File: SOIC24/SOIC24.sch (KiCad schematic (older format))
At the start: 5 parts, among them J1 Conn_01x12, J2 Conn_02x12_Counter_Clockwise, J3 Conn_02x12_Counter_Clockwise, J4 Conn_02x12_Counter_Clockwise, J5 Conn_01x12

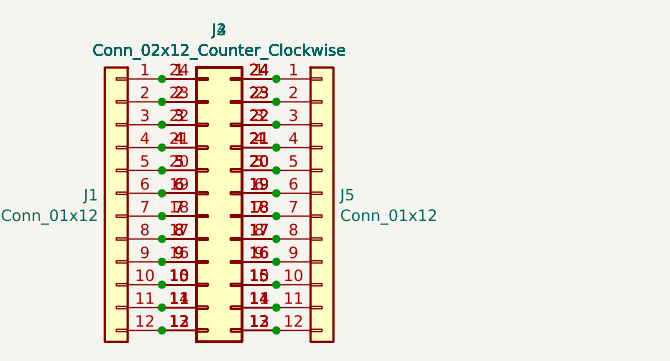
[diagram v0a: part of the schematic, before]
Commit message: Silkscreens and sizes updated
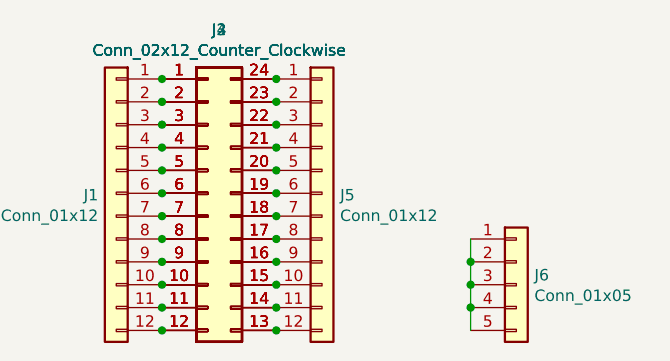
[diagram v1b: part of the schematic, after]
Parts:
- added J6: Conn_01x05, Connector_PinHeader_2.54mm:PinHeader_1x05_P2.54mm_Vertical, symbol Connector_Generic:Conn_01x05
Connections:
- net at J2.24 (Pin_24), J3.24 (Pin_24), J5.1 (Pin_1): now also J4.24 (Pin_24); no longer J4.1 (Pin_1)
- net at J2.15 (Pin_15), J3.15 (Pin_15), J5.10 (Pin_10): now also J4.15 (Pin_15); no longer J4.10 (Pin_10)
- net at J2.14 (Pin_14), J3.14 (Pin_14), J5.11 (Pin_11): now also J4.14 (Pin_14); no longer J4.11 (Pin_11)
- net at J2.13 (Pin_13), J3.13 (Pin_13), J5.12 (Pin_12): now also J4.13 (Pin_13); no longer J4.12 (Pin_12)
- net at J2.23 (Pin_23), J3.23 (Pin_23), J5.2 (Pin_2): now also J4.23 (Pin_23); no longer J4.2 (Pin_2)
- net at J2.22 (Pin_22), J3.22 (Pin_22), J5.3 (Pin_3): now also J4.22 (Pin_22); no longer J4.3 (Pin_3)
- net at J2.21 (Pin_21), J3.21 (Pin_21), J5.4 (Pin_4): now also J4.21 (Pin_21); no longer J4.4 (Pin_4)
- net at J2.20 (Pin_20), J3.20 (Pin_20), J5.5 (Pin_5): now also J4.20 (Pin_20); no longer J4.5 (Pin_5)
- net at J2.19 (Pin_19), J3.19 (Pin_19), J5.6 (Pin_6): now also J4.19 (Pin_19); no longer J4.6 (Pin_6)
- net at J2.18 (Pin_18), J3.18 (Pin_18), J5.7 (Pin_7): now also J4.18 (Pin_18); no longer J4.7 (Pin_7)
- net at J2.17 (Pin_17), J3.17 (Pin_17), J5.8 (Pin_8): now also J4.17 (Pin_17); no longer J4.8 (Pin_8)
- net at J2.16 (Pin_16), J3.16 (Pin_16), J5.9 (Pin_9): now also J4.16 (Pin_16); no longer J4.9 (Pin_9)
- net at J1.1 (Pin_1), J2.1 (Pin_1), J3.1 (Pin_1): now also J4.1 (Pin_1); no longer J4.24 (Pin_24)
- net at J1.10 (Pin_10), J2.10 (Pin_10), J3.10 (Pin_10): now also J4.10 (Pin_10); no longer J4.15 (Pin_15)
- net at J1.11 (Pin_11), J2.11 (Pin_11), J3.11 (Pin_11): now also J4.11 (Pin_11); no longer J4.14 (Pin_14)
- net at J1.12 (Pin_12), J2.12 (Pin_12), J3.12 (Pin_12): now also J4.12 (Pin_12); no longer J4.13 (Pin_13)
- net at J1.2 (Pin_2), J2.2 (Pin_2), J3.2 (Pin_2): now also J4.2 (Pin_2); no longer J4.23 (Pin_23)
- net at J1.3 (Pin_3), J2.3 (Pin_3), J3.3 (Pin_3): now also J4.3 (Pin_3); no longer J4.22 (Pin_22)
- net at J1.4 (Pin_4), J2.4 (Pin_4), J3.4 (Pin_4): now also J4.4 (Pin_4); no longer J4.21 (Pin_21)
- net at J1.5 (Pin_5), J2.5 (Pin_5), J3.5 (Pin_5): now also J4.5 (Pin_5); no longer J4.20 (Pin_20)
- net at J1.6 (Pin_6), J2.6 (Pin_6), J3.6 (Pin_6): now also J4.6 (Pin_6); no longer J4.19 (Pin_19)
- net at J1.7 (Pin_7), J2.7 (Pin_7), J3.7 (Pin_7): now also J4.7 (Pin_7); no longer J4.18 (Pin_18)
- net at J1.8 (Pin_8), J2.8 (Pin_8), J3.8 (Pin_8): now also J4.8 (Pin_8); no longer J4.17 (Pin_17)
- net at J1.9 (Pin_9), J2.9 (Pin_9), J3.9 (Pin_9): now also J4.9 (Pin_9); no longer J4.16 (Pin_16)
- new net: J6.1 (Pin_1), J6.2 (Pin_2), J6.3 (Pin_3), J6.4 (Pin_4), J6.5 (Pin_5)
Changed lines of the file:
@@
 EESchema Schematic File Version 4
-LIBS:SOIC28-cache
+LIBS:SOIC24-cache
 EELAYER 29 0
 EELAYER END
@@
 $EndComp
 $Comp
-L Connector_Generic:Conn_02x12_Counter_Clockwise J4
-U 1 1 5D376A89
-P 6450 3700
-F 0 "J4" H 6500 4415 50  0000 C CNN
-F 1 "Conn_02x12_Counter_Clockwise" H 6500 4325 50  0000 C CNN
-F 2 "Package_DFN_QFN:QFN-24-1EP_5x5mm_P0.65mm_EP3.4x3.4mm" H 6450 3700 50  0001 C CNN
-F 3 "~" H 6450 3700 50  0001 C CNN
-	1    6450 3700
-	-1   0    0    -1
-$EndComp
-$Comp
-L Connector_Generic:Conn_02x12_Counter_Clockwise J2
-U 1 1 5D378DEE
-P 6350 3700
-F 0 "J2" H 6400 4415 50  0000 C CNN
-F 1 "Conn_02x12_Counter_Clockwise" H 6400 4325 50  0000 C CNN
-F 2 "Package_DFN_QFN:QFN-24-1EP_3x3mm_P0.4mm_EP1.75x1.6mm" H 6350 3700 50  0001 C CNN
-F 3 "~" H 6350 3700 50  0001 C CNN
-	1    6350 3700
-	1    0    0    -1
-$EndComp
-$Comp
 L Connector_Generic:Conn_02x12_Counter_Clockwise J3
 U 1 1 5D379B2C
@@
 F 1 "Conn_02x12_Counter_Clockwise" H 6400 4325 50  0000 C CNN
 F 2 "Package_SO:SOIC-24W_7.5x15.4mm_P1.27mm" H 6350 3700 50  0001 C CNN
+F 3 "~" H 6350 3700 50  0001 C CNN
+	1    6350 3700
+	1    0    0    -1
+$EndComp
+$Comp
+L Connector_Generic:Conn_02x12_Counter_Clockwise J2
+U 1 1 5D3AA382
+P 6350 3700
+F 0 "J2" H 6400 4415 50  0000 C CNN
+F 1 "Conn_02x12_Counter_Clockwise" H 6400 4325 50  0000 C CNN
+F 2 "Package_DFN_QFN:QFN-24-1EP_3x3mm_P0.4mm_EP1.75x1.6mm" H 6350 3700 50  0001 C CNN
 F 3 "~" H 6350 3700 50  0001 C CNN
 	1    6350 3700
@@
 Connection ~ 6650 4200
 Connection ~ 6650 4300
+$Comp
+L Connector_Generic:Conn_02x12_Counter_Clockwise J4
+U 1 1 5D3AD66F
+P 6350 3700
+F 0 "J4" H 6400 4415 50  0000 C CNN
+F 1 "Conn_02x12_Counter_Clockwise" H 6400 4325 50  0000 C CNN
+F 2 "Package_DFN_QFN:QFN-24-1EP_5x5mm_P0.65mm_EP3.4x3.4mm" H 6350 3700 50  0001 C CNN
+F 3 "~" H 6350 3700 50  0001 C CNN
+	1    6350 3700
+	1    0    0    -1
+$EndComp
+$Comp
+L Connector_Generic:Conn_01x05 J6
+U 1 1 5D3D3EBE
+P 7700 4100
+F 0 "J6" H 7779 4142 50  0000 L CNN
+F 1 "Conn_01x05" H 7779 4052 50  0000 L CNN
+F 2 "Connector_PinHeader_2.54mm:PinHeader_1x05_P2.54mm_Vertical" H 7700 4100 50  0001 C CNN
+F 3 "~" H 7700 4100 50  0001 C CNN
+	1    7700 4100
+	1    0    0    -1
+$EndComp
+Wire Wire Line
+	7500 4300 7500 4200
+Connection ~ 7500 4000
+Wire Wire Line
+	7500 4000 7500 3900
+Connection ~ 7500 4100
+Wire Wire Line
+	7500 4100 7500 4000
+Connection ~ 7500 4200
+Wire Wire Line
+	7500 4200 7500 4100
 $EndSCHEMATC

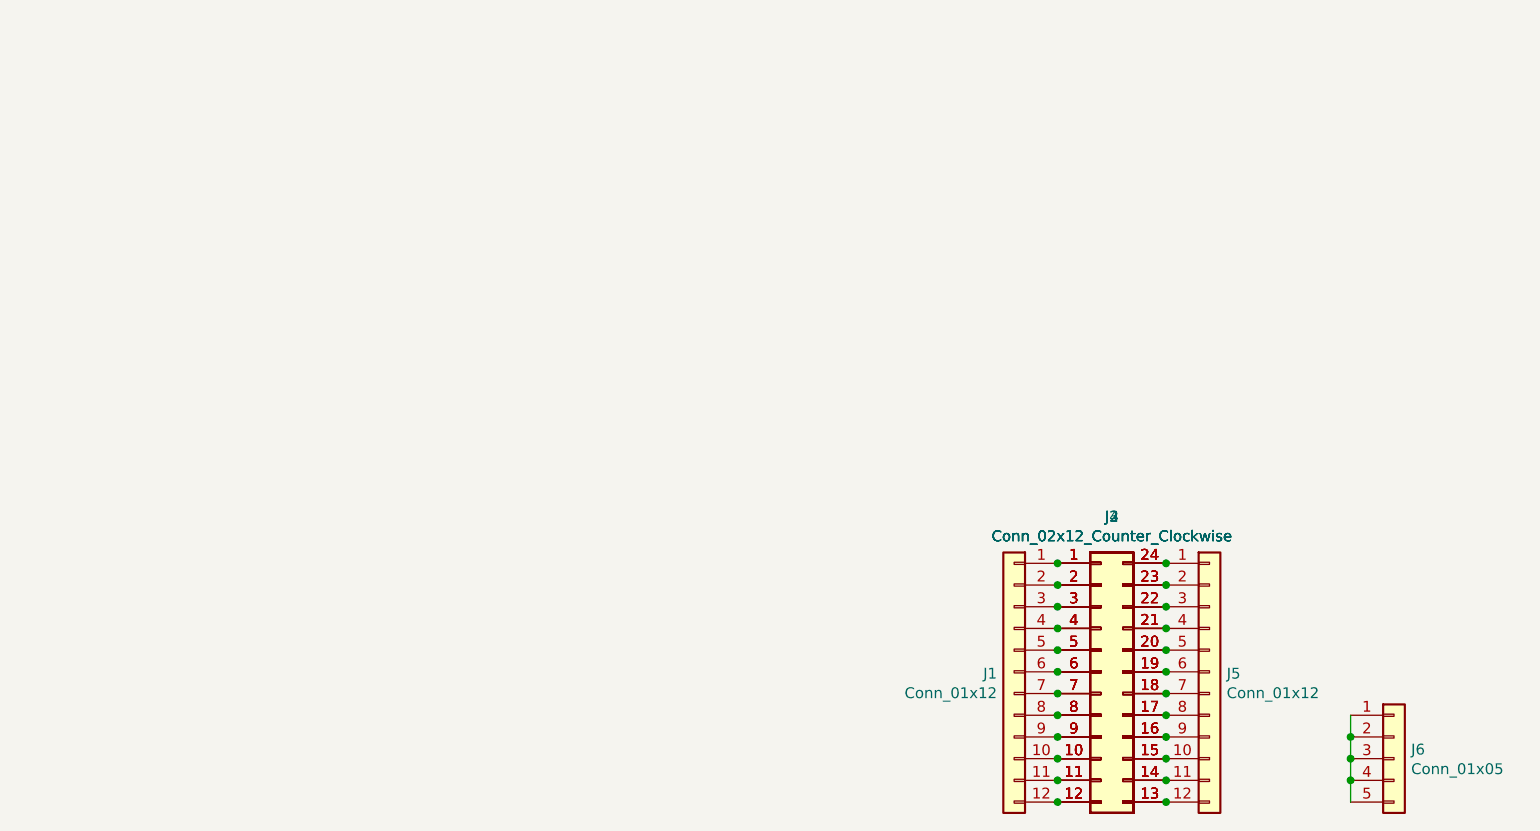
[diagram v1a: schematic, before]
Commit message: USB, SD and CR Cells Added
MicroSD, MicroUSB, MiniUSB, USB-C, CR1220, CR2032 added as well as all schematics page sizes optimised
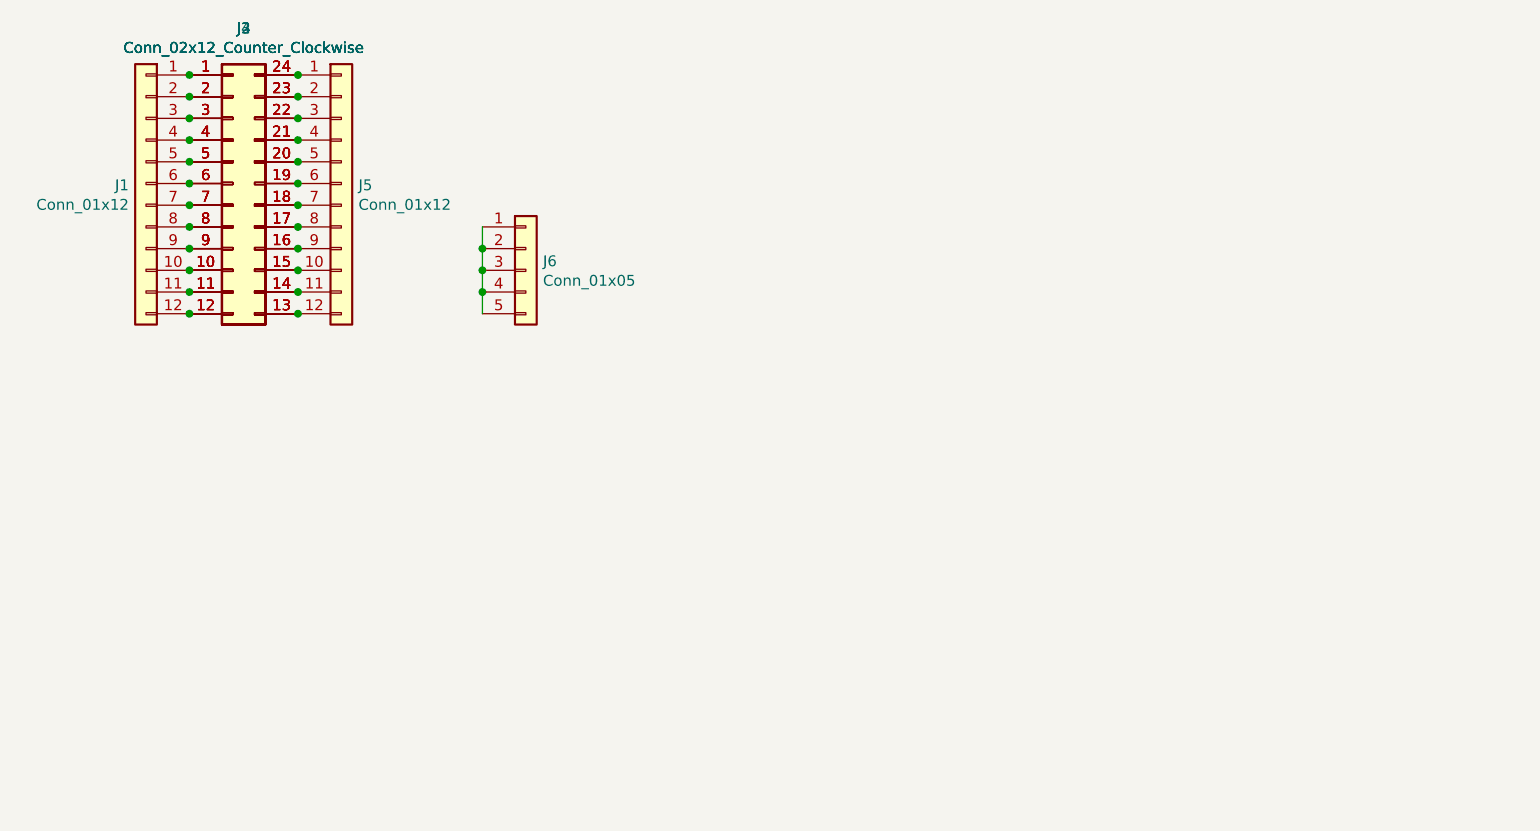
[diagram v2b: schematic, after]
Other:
- moved on the sheet: J1, J2, J3, J4, J5, J6
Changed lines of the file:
@@
 EELAYER 29 0
 EELAYER END
-$Descr A4 11693 8268
+$Descr User 5197 4016
 encoding utf-8
 Sheet 1 1
-Title ""
-Date ""
-Rev ""
-Comp ""
-Comment1 ""
-Comment2 ""
-Comment3 ""
-Comment4 ""
+Title "SOIC24 To DIP24 Breakout Board"
+Date "2019-07-23"
+Rev "1"
+Comp "SirBoard"
+Comment1 "SOIC24 P = 1.27mm"
+Comment2 "QFN24 P = 0.65mm"
+Comment3 "QFN24 P = 0.4mm"
+Comment4 "DIP24 P = 2.54mm"
 $EndDescr
 $Comp
 L Connector_Generic:Conn_01x12 J5
 U 1 1 5D373AE3
-P 6850 3700
-F 0 "J5" H 6929 3692 50  0000 L CNN
-F 1 "Conn_01x12" H 6929 3602 50  0000 L CNN
-F 2 "Connector_PinHeader_2.54mm:PinHeader_1x12_P2.54mm_Vertical" H 6850 3700 50  0001 C CNN
-F 3 "~" H 6850 3700 50  0001 C CNN
-	1    6850 3700
+P 2850 1450
+F 0 "J5" H 2929 1442 50  0000 L CNN
+F 1 "Conn_01x12" H 2929 1352 50  0000 L CNN
+F 2 "Connector_PinHeader_2.54mm:PinHeader_1x12_P2.54mm_Vertical" H 2850 1450 50  0001 C CNN
+F 3 "~" H 2850 1450 50  0001 C CNN
+	1    2850 1450
 	1    0    0    -1
 $EndComp
@@
 L Connector_Generic:Conn_01x12 J1
 U 1 1 5D37609B
-P 5950 3700
-F 0 "J1" H 6029 3692 50  0000 L CNN
-F 1 "Conn_01x12" H 6029 3602 50  0000 L CNN
-F 2 "Connector_PinHeader_2.54mm:PinHeader_1x12_P2.54mm_Vertical" H 5950 3700 50  0001 C CNN
-F 3 "~" H 5950 3700 50  0001 C CNN
-	1    5950 3700
+P 1950 1450
+F 0 "J1" H 2029 1442 50  0000 L CNN
+F 1 "Conn_01x12" H 2029 1352 50  0000 L CNN
+F 2 "Connector_PinHeader_2.54mm:PinHeader_1x12_P2.54mm_Vertical" H 1950 1450 50  0001 C CNN
+F 3 "~" H 1950 1450 50  0001 C CNN
+	1    1950 1450
 	-1   0    0    -1
 $EndComp
@@
 L Connector_Generic:Conn_02x12_Counter_Clockwise J3
 U 1 1 5D379B2C
-P 6350 3700
-F 0 "J3" H 6400 4415 50  0000 C CNN
-F 1 "Conn_02x12_Counter_Clockwise" H 6400 4325 50  0000 C CNN
-F 2 "Package_SO:SOIC-24W_7.5x15.4mm_P1.27mm" H 6350 3700 50  0001 C CNN
-F 3 "~" H 6350 3700 50  0001 C CNN
-	1    6350 3700
+P 2350 1450
+F 0 "J3" H 2400 2165 50  0000 C CNN
+F 1 "Conn_02x12_Counter_Clockwise" H 2400 2075 50  0000 C CNN
+F 2 "Package_SO:SOIC-24W_7.5x15.4mm_P1.27mm" H 2350 1450 50  0001 C CNN
+F 3 "~" H 2350 1450 50  0001 C CNN
+	1    2350 1450
 	1    0    0    -1
 $EndComp
@@
 L Connector_Generic:Conn_02x12_Counter_Clockwise J2
 U 1 1 5D3AA382
-P 6350 3700
-F 0 "J2" H 6400 4415 50  0000 C CNN
-F 1 "Conn_02x12_Counter_Clockwise" H 6400 4325 50  0000 C CNN
-F 2 "Package_DFN_QFN:QFN-24-1EP_3x3mm_P0.4mm_EP1.75x1.6mm" H 6350 3700 50  0001 C CNN
-F 3 "~" H 6350 3700 50  0001 C CNN
-	1    6350 3700
+P 2350 1450
+F 0 "J2" H 2400 2165 50  0000 C CNN
+F 1 "Conn_02x12_Counter_Clockwise" H 2400 2075 50  0000 C CNN
+F 2 "Package_DFN_QFN:QFN-24-1EP_3x3mm_P0.4mm_EP1.75x1.6mm" H 2350 1450 50  0001 C CNN
+F 3 "~" H 2350 1450 50  0001 C CNN
+	1    2350 1450
 	1    0    0    -1
 $EndComp
-Connection ~ 6150 3200
-Connection ~ 6150 3300
-Connection ~ 6150 3400
-Connection ~ 6150 3500
-Connection ~ 6150 3600
-Connection ~ 6150 3700
-Connection ~ 6150 3800
-Connection ~ 6150 3900
-Connection ~ 6150 4000
-Connection ~ 6150 4100
-Connection ~ 6150 4200
-Connection ~ 6150 4300
-Connection ~ 6650 3200
-Connection ~ 6650 3300
-Connection ~ 6650 3400
-Connection ~ 6650 3500
-Connection ~ 6650 3600
-Connection ~ 6650 3700
-Connection ~ 6650 3800
-Connection ~ 6650 3900
-Connection ~ 6650 4000
-Connection ~ 6650 4100
-Connection ~ 6650 4200
-Connection ~ 6650 4300
+Connection ~ 2150 950
+Connection ~ 2150 1050
+Connection ~ 2150 1150
+Connection ~ 2150 1250
+Connection ~ 2150 1350
+Connection ~ 2150 1450
+Connection ~ 2150 1550
+Connection ~ 2150 1650
+Connection ~ 2150 1750
+Connection ~ 2150 1850
+Connection ~ 2150 1950
+Connection ~ 2150 2050
+Connection ~ 2650 950
+Connection ~ 2650 1050
+Connection ~ 2650 1150
+Connection ~ 2650 1250
+Connection ~ 2650 1350
+Connection ~ 2650 1450
+Connection ~ 2650 1550
+Connection ~ 2650 1650
+Connection ~ 2650 1750
+Connection ~ 2650 1850
+Connection ~ 2650 1950
+Connection ~ 2650 2050
 $Comp
 L Connector_Generic:Conn_02x12_Counter_Clockwise J4
 U 1 1 5D3AD66F
-P 6350 3700
-F 0 "J4" H 6400 4415 50  0000 C CNN
-F 1 "Conn_02x12_Counter_Clockwise" H 6400 4325 50  0000 C CNN
-F 2 "Package_DFN_QFN:QFN-24-1EP_5x5mm_P0.65mm_EP3.4x3.4mm" H 6350 3700 50  0001 C CNN
-F 3 "~" H 6350 3700 50  0001 C CNN
-	1    6350 3700
+P 2350 1450
+F 0 "J4" H 2400 2165 50  0000 C CNN
+F 1 "Conn_02x12_Counter_Clockwise" H 2400 2075 50  0000 C CNN
+F 2 "Package_DFN_QFN:QFN-24-1EP_5x5mm_P0.65mm_EP3.4x3.4mm" H 2350 1450 50  0001 C CNN
+F 3 "~" H 2350 1450 50  0001 C CNN
+	1    2350 1450
 	1    0    0    -1
 $EndComp
@@
 L Connector_Generic:Conn_01x05 J6
 U 1 1 5D3D3EBE
-P 7700 4100
-F 0 "J6" H 7779 4142 50  0000 L CNN
-F 1 "Conn_01x05" H 7779 4052 50  0000 L CNN
-F 2 "Connector_PinHeader_2.54mm:PinHeader_1x05_P2.54mm_Vertical" H 7700 4100 50  0001 C CNN
-F 3 "~" H 7700 4100 50  0001 C CNN
-	1    7700 4100
+P 3700 1850
+F 0 "J6" H 3779 1892 50  0000 L CNN
+F 1 "Conn_01x05" H 3779 1802 50  0000 L CNN
+F 2 "Connector_PinHeader_2.54mm:PinHeader_1x05_P2.54mm_Vertical" H 3700 1850 50  0001 C CNN
+F 3 "~" H 3700 1850 50  0001 C CNN
+	1    3700 1850
 	1    0    0    -1
 $EndComp
 Wire Wire Line
-	7500 4300 7500 4200
-Connection ~ 7500 4000
+	3500 2050 3500 1950
+Connection ~ 3500 1750
 Wire Wire Line
-	7500 4000 7500 3900
-Connection ~ 7500 4100
+	3500 1750 3500 1650
+Connection ~ 3500 1850
 Wire Wire Line
-	7500 4100 7500 4000
-Connection ~ 7500 4200
+	3500 1850 3500 1750
+Connection ~ 3500 1950
 Wire Wire Line
-	7500 4200 7500 4100
+	3500 1950 3500 1850
 $EndSCHEMATC
